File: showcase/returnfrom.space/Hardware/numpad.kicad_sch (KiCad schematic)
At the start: 52 parts, among them J21 Conn_01x08_Socket, J22 USB_C_Receptacle_USB2.0_16P, SW1 SW_SPST, SW10 SW_SPST, SW11 SW_SPST, SW12 SW_SPST, SW13 SW_SPST, SW14 SW_SPST, SW15 SW_SPST, SW16 SW_SPST, SW17 RESET, SW18 BOOTSEL, SW2 SW_SPST, SW3 SW_SPST, SW4 SW_SPST, SW5 SW_SPST, SW6 SW_SPST, SW7 SW_SPST, SW8 SW_SPST, SW9 SW_SPST, U3 RP2040, U8 W25Q128JVS

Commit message: added step files
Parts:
- added C12, C13, C14, C15, C16, C17, C18: 100nF, Capacitor_SMD:C_0402_1005Metric, symbol Device:C
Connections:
- net GND: now also C12.1, C13.1, C14.2, C15.2, C16.2, C17.2, C18.1
- net at U3.1 (IOVDD), U3.10 (IOVDD), U3.22 (IOVDD)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: now also C17.1
- net at U3.23 (DVDD), U3.50 (DVDD): now also C13.2
- net at U3.43 (ADC_AVDD): now also C15.1
- net at U3.44 (VREG_IN): now also C14.1
- net at U3.45 (VREG_VOUT): now also C12.2
- net at U3.48 (USB_VDD): now also C16.1

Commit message: updated
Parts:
- removed J15, J19: ~, spacescape:Untitled, symbol spacescape:RES-PAD
- added BOOT1, GND1, IO16, RGB+1, RGB-1, RGB1, RST1, SWCLK1, SWD1: TestPoint, TestPoint:TestPoint_Pad_D2.0mm, symbol Connector:TestPoint
- added C19, C20: 15pF, Capacitor_SMD:C_0402_1005Metric, symbol Device:C
- added C21, C25, C26: 100nF, Capacitor_SMD:C_0402_1005Metric, symbol Device:C
- added C22, C23, C24, C28, C39: 1uF, Capacitor_SMD:C_0402_1005Metric, symbol Device:C
- added C35, C36: 22uF, Capacitor_SMD:C_0805_2012Metric, symbol Device:C
- added D10, D11, D12, D13, D4, D5, D6, D7, D8, D9: WS2812B-2020, LED_SMD:LED_WS2812B-2020_PLCC4_2.0x2.0mm, symbol LED:WS2812B-2020
- added J7: OLED, TG9541:Display_128x64_096_I2C, symbol Connector:Conn_01x04_Socket
- added Q1: Crystal_GND24, Crystal:Crystal_SMD_3225-4Pin_3.2x2.5mm, symbol Device:Crystal_GND24
- added R24, R25, R37: 27R, Resistor_SMD:R_0402_1005Metric, symbol Device:R
- added R38, R39: 5K1, Resistor_SMD:R_0402_1005Metric, symbol Device:R
- added U1: AMS1117-3.3, Package_TO_SOT_SMD:SOT-223-3_TabPin2, symbol Regulator_Linear:AMS1117-3.3
- C13: renamed from C12; value 100nF -> 1uF
- C14: value 100nF -> 1uF
- R15, R16: value 330 -> 27R
- renumbered C13 to C12
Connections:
- net +3.3V is gone; now on net +3V3: C6.1, J21.3 (Pin_3), R17.2, R18.2, U8.8 (VCC)
- net +5V: now also J21.1 (Pin_1), U1.3 (VI); no longer J21.2 (Pin_2)
- net DM1: now also R24.1; no longer J22.A7 (D-), J22.B7 (D-)
- net DP1: now also R25.1; no longer J22.A6 (D+), J22.B6 (D+)
- net GND: now also U3.19 (TESTEN), C19.2, C20.2, C21.2, C22.1, C23.1, C24.1, C25.2, C26.2, C28.1, C35.2, C36.2, C39.2, D10.2 (VSS), D11.2 (VSS), D12.2 (VSS), D13.2 (VSS), D4.2 (VSS), D5.2 (VSS), D6.2 (VSS), D7.2 (VSS), D8.2 (VSS), D9.2 (VSS), GND1.1, J7.1 (Pin_1), Q1.2, Q1.4, RGB-1.1, U1.1 (GND)
- net at SW10.1 (A), SW14.1 (A), SW2.1 (A)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: now also U3.16 (GPIO13); no longer U3.7 (GPIO5)
- net at SW13.2 (B), SW14.2 (B), SW15.2 (B)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: now also R5.1; no longer R8.1
- net at SW1.1 (A), SW13.1 (A), SW5.1 (A)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: now also U3.15 (GPIO12); no longer U3.6 (GPIO4)
- net at SW5.2 (B), SW6.2 (B), SW7.2 (B)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: now also R7.1; no longer R6.1
- net at SW11.1 (A), SW15.1 (A), SW3.1 (A)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: now also U3.17 (GPIO14); no longer U3.8 (GPIO6)
- net at J12.A: now also U3.8 (GPIO6); no longer U3.29 (GPIO18)
- net at J14.A: now also U3.34 (GPIO22); no longer U3.31 (GPIO20)
- net at J13.A: now also U3.37 (GPIO25); no longer U3.30 (GPIO19)
- net at J16.A: now also U3.7 (GPIO5); no longer U3.34 (GPIO22)
- net at SW12.1 (A), SW16.1 (A), SW4.1 (A)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: now also U3.18 (GPIO15); no longer U3.9 (GPIO7)
- net +1V1: now reaches C12.2, U3.23 (DVDD), U3.50 (DVDD)
- net +1V1: now also C13.2, C18.2, U3.45 (VREG_VOUT)
- net +3V3: now reaches C17.1, U3.1 (IOVDD), U3.10 (IOVDD), U3.22 (IOVDD), U3.33 (IOVDD), U3.42 (IOVDD), U3.49 (IOVDD)
- net +3V3: now also C14.1, C15.1, C16.1, U3.43 (ADC_AVDD), U3.44 (VREG_IN), U3.48 (USB_VDD), C21.1, C22.2, C23.2, C24.2, C25.1, C26.1, C28.2, C35.1, C36.1, C39.1, D10.4 (VDD), D11.4 (VDD), D12.4 (VDD), D13.4 (VDD), D4.4 (VDD), D5.4 (VDD), D6.4 (VDD), D7.4 (VDD), D8.4 (VDD), D9.4 (VDD), J7.2 (Pin_2), R38.1, R39.2, RGB+1.1, U1.2 (VO)
- net at J8.A: now also U3.9 (GPIO7); no longer U3.17 (GPIO14)
- net at J9.A: now also U3.6 (GPIO4); no longer U3.18 (GPIO15)
- net at U3.20 (XIN): now also C19.1, Q1.3
- net at U3.21 (XOUT): now also C20.1, Q1.1
- net at U3.24 (SWCLK): now also SWCLK1.1
- net at U3.25 (SWD): now also SWD1.1
- net RST1: now reaches C7.2, R18.1, SW17.2 (B), U3.26 (RUN)
- net RST1: now also J21.2 (Pin_2), RST1.1
- net at U3.27 (GPIO16): now also IO16.1; no longer J10.A
- net at J11.A: now also U3.31 (GPIO20); no longer U3.28 (GPIO17)
- net at U3.32 (GPIO21): now also J18.A
- net at U3.35 (GPIO23): now also J10.A; no longer J17.A
- net at U3.36 (GPIO24): now also J17.A; no longer J18.A
- net BOOT1: now reaches C8.2, R17.1, SW18.2 (B), U3.56 (QSPI_SS), U8.1 (~{CS})
- net BOOT1: now also BOOT1.1
- net at SW1.2 (B), SW2.2 (B), SW3.2 (B)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: now also R8.1; no longer R5.1
- net at SW10.2 (B), SW11.2 (B), SW12.2 (B)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: now also R6.1; no longer R7.1
- new net: D8.1 (DOUT), D9.3 (DIN)
- new net: D7.1 (DOUT), D8.3 (DIN)
- new net: D5.1 (DOUT), D6.3 (DIN)
- new net: D4.1 (DOUT), D5.3 (DIN)
- new net: D4.3 (DIN), R37.1
- new net: D13.1 (DOUT), RGB1.1
- new net: D6.1 (DOUT), D7.3 (DIN)
- new net: J22.A6 (D+), J22.B6 (D+), R25.2
- new net: J22.A7 (D-), J22.B7 (D-), R24.2
- new net: D12.1 (DOUT), D13.3 (DIN)
- new net: D11.1 (DOUT), D12.3 (DIN)
- new net: D10.3 (DIN), D9.1 (DOUT)
- new net: D10.1 (DOUT), D11.3 (DIN)
- new net RGB: R37.2, U3.28 (GPIO17)
- new net RPSCL: J7.3 (Pin_3), R39.1, U3.29 (GPIO18)
- new net RPSDA: J7.4 (Pin_4), R38.2, U3.30 (GPIO19)
- no-connect marks 0 -> 5
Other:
- moved on the sheet: C10, C11, C12, C13, C14, C15, C16, C17, C18, C6, C7, C8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

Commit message: updated
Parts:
- added D16, D17: RED LED, LED_SMD:LED_0603_1608Metric, symbol Device:LED
- added R51, R55, R56: 1K, Resistor_SMD:R_0402_1005Metric, symbol Device:R
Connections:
- net +3V3: now also D16.2 (A)
- net GND: now also R55.2, R56.2
- net IO6: now reaches J12.A, U3.8 (GPIO6)
- net IO5: now reaches J16.A, U3.7 (GPIO5)
- net IO8: now reaches R5.2, U3.11 (GPIO8)
- net IO9: now reaches R6.2, U3.12 (GPIO9)
- net IO0: now reaches J21.5 (Pin_5), U3.2 (GPIO0)
- net IO1: now reaches J21.6 (Pin_6), U3.3 (GPIO1)
- net at U3.39 (GPIO27_ADC1): now also D17.2 (A)
- net IO2: now reaches J21.7 (Pin_7), U3.4 (GPIO2)
- net ADC3: now reaches U3.41 (GPIO29_ADC3)
- net ADC3: now also R51.1
- net IO3: now reaches J21.8 (Pin_8), U3.5 (GPIO3)
- net IO4: now reaches J9.A, U3.6 (GPIO4)
- net IO7: now reaches J8.A, U3.9 (GPIO7)
- new net: D17.1 (K), R56.1
- new net: D16.1 (K), R55.1
- no-connect marks 5 -> 3
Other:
- moved on the sheet: J21, R4

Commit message: board almost done
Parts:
- added Q5: NPN, Package_TO_SOT_SMD:SOT-23, symbol Simulation_SPICE:NPN
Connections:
- net GND: now also Q5.3 (E)
- net RST1: now also Q5.1 (C); no longer J21.2 (Pin_2)
- new net: J21.2 (Pin_2), Q5.2 (B)
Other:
- moved on the sheet: J21

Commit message: panelizing...
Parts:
- added ADC3: TestPoint, TestPoint:TestPoint_Pad_D2.0mm, symbol Connector:TestPoint
- J10, J11, J12, J13, J14, J16, J17, J18, J8, J9: footprint spacescape:Untitled -> spacescape:RES-PAD
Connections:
- net IO13: now reaches SW10.1 (A), SW14.1 (A), SW2.1 (A), SW6.1 (A), U3.16 (GPIO13)
- net IO12: now reaches SW1.1 (A), SW13.1 (A), SW5.1 (A), SW9.1 (A), U3.15 (GPIO12)
- net IO14: now reaches SW11.1 (A), SW15.1 (A), SW3.1 (A), SW7.1 (A), U3.17 (GPIO14)
- net at R51.2: now also ADC3.1
- net IO15: now reaches SW12.1 (A), SW16.1 (A), SW4.1 (A), SW8.1 (A), U3.18 (GPIO15)
- net IO10: now reaches R7.2, U3.13 (GPIO10)
- net IO11: now reaches R8.2, U3.14 (GPIO11)
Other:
- moved on the sheet: IO16, R51

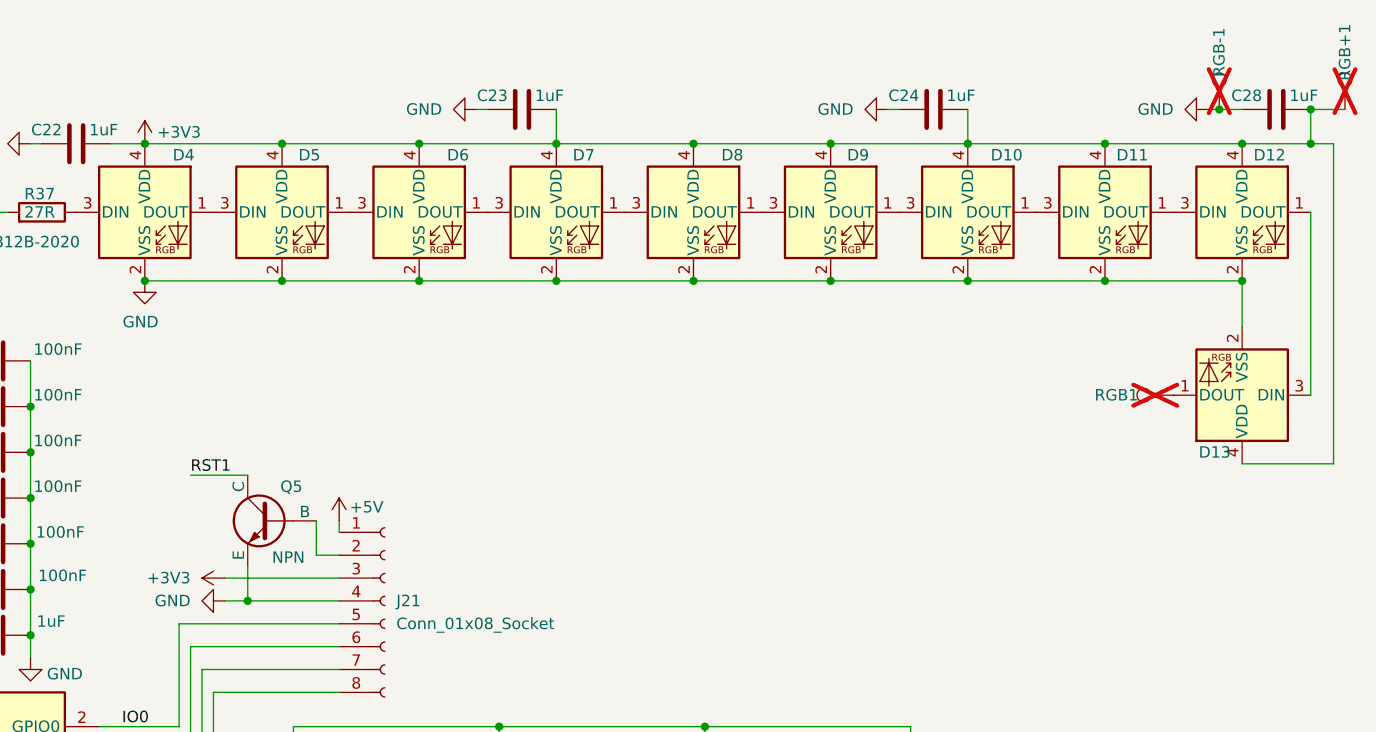
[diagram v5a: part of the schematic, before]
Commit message: Done. Ordered 50pcs. TO DO: clean-up, add BOM & POS
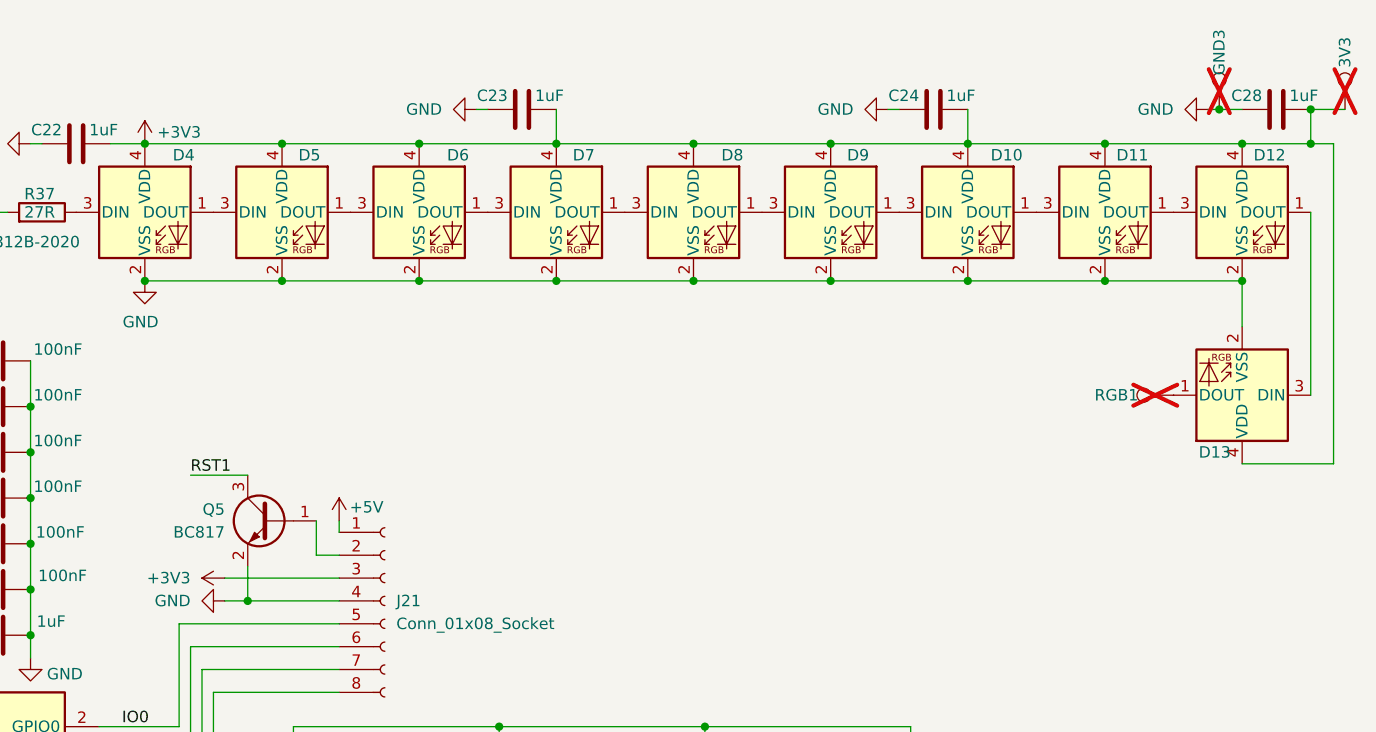
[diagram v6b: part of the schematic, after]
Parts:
- removed Q5: NPN, Package_TO_SOT_SMD:SOT-23, symbol Simulation_SPICE:NPN
- added Q5: BC817, Package_TO_SOT_SMD:SOT-23, symbol Transistor_BJT:BC817
- SW11: 3D (none) -> ${KICAD9_3DMODEL_DIR}/Button_Switch_SMD.3dshapes/SW_SPST_TL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
- renumbered RGB+1 to 3V3, RGB-1 to GND3
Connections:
- net GND: now also Q5.2 (E)
- net RST1: now also Q5.3 (C)
- net at J21.2 (Pin_2): now also Q5.1 (B)
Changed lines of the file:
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@@
 		(on_board yes)
 		(dnp yes)
-		(property "Reference" "RGB+1"
+		(property "Reference" "3V3"
 			(at 276.86 22.86 90)
 			(effects
@@
 			(project "spacescape"
 				(path "/418a52ba-b136-48f0-a485-149e9dc1363e/b3767966-d6d1-4f79-8708-552c7bb7a812"
-					(reference "RGB+1")
+					(reference "3V3")
 					(unit 1)
 				)
@@
 	)
 	(symbol
+		(lib_id "Transistor_BJT:BC817")
+		(at 157.48 74.93 0)
+		(mirror y)
+		(unit 1)
+		(exclude_from_sim no)
+		(in_bom yes)
+		(on_board yes)
+		(dnp no)
+		(property "Reference" "Q5"
+			(at 152.4 73.6599 0)
+			(effects
+				(font
+					(size 1.27 1.27)
+				)
+				(justify left)
+			)
+		)
+		(property "Value" "BC817"
+			(at 152.4 76.1999 0)
+			(effects
+				(font
+					(size 1.27 1.27)
+				)
+				(justify left)
+			)
+		)
+		(property "Footprint" "Package_TO_SOT_SMD:SOT-23"
+			(at 152.4 76.835 0)
+			(effects
+				(font
+					(size 1.27 1.27)
+					(italic yes)
+				)
+				(justify left)
+				(hide yes)
+			)
+		)
+		(property "Datasheet" "https://www.onsemi.com/pub/Collateral/BC818-D.pdf"
+			(at 157.48 74.93 0)
+			(effects
+				(font
+					(size 1.27 1.27)
+				)
+				(justify left)
+				(hide yes)
+			)
+		)
+		(property "Description" "0.8A Ic, 45V Vce, NPN Transistor, SOT-23"
+			(at 157.48 74.93 0)
+			(effects
+				(font
+					(size 1.27 1.27)
+				)
+				(hide yes)
+			)
+		)
+		(pin "3"
+		)
+		(pin "2"
+		)
+		(pin "1"
+		)
+		(instances
+			(project "spacescape"
+				(path "/418a52ba-b136-48f0-a485-149e9dc1363e/b3767966-d6d1-4f79-8708-552c7bb7a812"
+					(reference "Q5")
+					(unit 1)
+				)
+			)
+		)
+	)
+	(symbol
 		(lib_id "power:+5V")
 		(at 109.22 33.02 0)
@@
 			)
 		)
+		(property "3D" "${KICAD9_3DMODEL_DIR}/Button_Switch_SMD.3dshapes/SW_SPST_TL3342.step"
+			(at 219.71 113.03 0)
+			(effects
+				(font
+					(size 1.27 1.27)
+				)
+				(hide yes)
+			)
+		)
 		(pin "1"
 		)
@@
 	)
 	(symbol
-		(lib_id "Simulation_SPICE:NPN")
-		(at 157.48 74.93 0)
-		(mirror y)
-		(unit 1)
-		(exclude_from_sim no)
-		(in_bom yes)
-		(on_board yes)
-		(dnp no)
-		(property "Reference" "Q5"
-			(at 161.036 71.12 0)
-			(effects
-				(font
-					(size 1.27 1.27)
-				)
-				(justify left)
-			)
-		)
-		(property "Value" "NPN"
-			(at 161.29 78.994 0)
-			(effects
-				(font
-					(size 1.27 1.27)
-				)
-				(justify left)
-			)
-		)
-		(property "Footprint" "Package_TO_SOT_SMD:SOT-23"
-			(at 93.98 74.93 0)
-			(effects
-				(font
-					(size 1.27 1.27)
-				)
-				(hide yes)
-			)
-		)
-		(property "Datasheet" "https://ngspice.sourceforge.io/docs/ngspice-html-manual/manual.xhtml#cha_BJTs"
-			(at 93.98 74.93 0)
-			(effects
-				(font
-					(size 1.27 1.27)
-				)
-				(hide yes)
-			)
-		)
-		(property "Description" "Bipolar transistor symbol for simulation only, substrate tied to the emitter"
-			(at 157.48 74.93 0)
-			(effects
-				(font
-					(size 1.27 1.27)
-				)
-				(hide yes)
-			)
-		)
-		(property "Sim.Device" "NPN"
-			(at 157.48 74.93 0)
-			(effects
-				(font
-					(size 1.27 1.27)
-				)
-				(hide yes)
-			)
-		)
-		(property "Sim.Type" "GUMMELPOON"
-			(at 157.48 74.93 0)
-			(effects
-				(font
-					(size 1.27 1.27)
-				)
-				(hide yes)
-			)
-		)
-		(property "Sim.Pins" "1=C 2=B 3=E"
-			(at 157.48 74.93 0)
-			(effects
-				(font
-					(size 1.27 1.27)
-				)
-				(hide yes)
-			)
-		)
-		(pin "2"
-		)
-		(pin "1"
-		)
-		(pin "3"
-		)
-		(instances
-			(project "spacescape"
-				(path "/418a52ba-b136-48f0-a485-149e9dc1363e/b3767966-d6d1-4f79-8708-552c7bb7a812"
-					(reference "Q5")
-					(unit 1)
-				)
-			)
-		)
-	)
-	(symbol
 		(lib_id "Device:C")
 		(at 185.42 29.21 90)
@@
 		(on_board yes)
 		(dnp yes)
-		(property "Reference" "RGB-1"
+		(property "Reference" "GND3"
 			(at 262.89 22.86 90)
 			(effects
@@
 			(project "spacescape"
 				(path "/418a52ba-b136-48f0-a485-149e9dc1363e/b3767966-d6d1-4f79-8708-552c7bb7a812"
-					(reference "RGB-1")
+					(reference "GND3")
 					(unit 1)
 				)
